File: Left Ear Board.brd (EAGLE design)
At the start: 5 parts

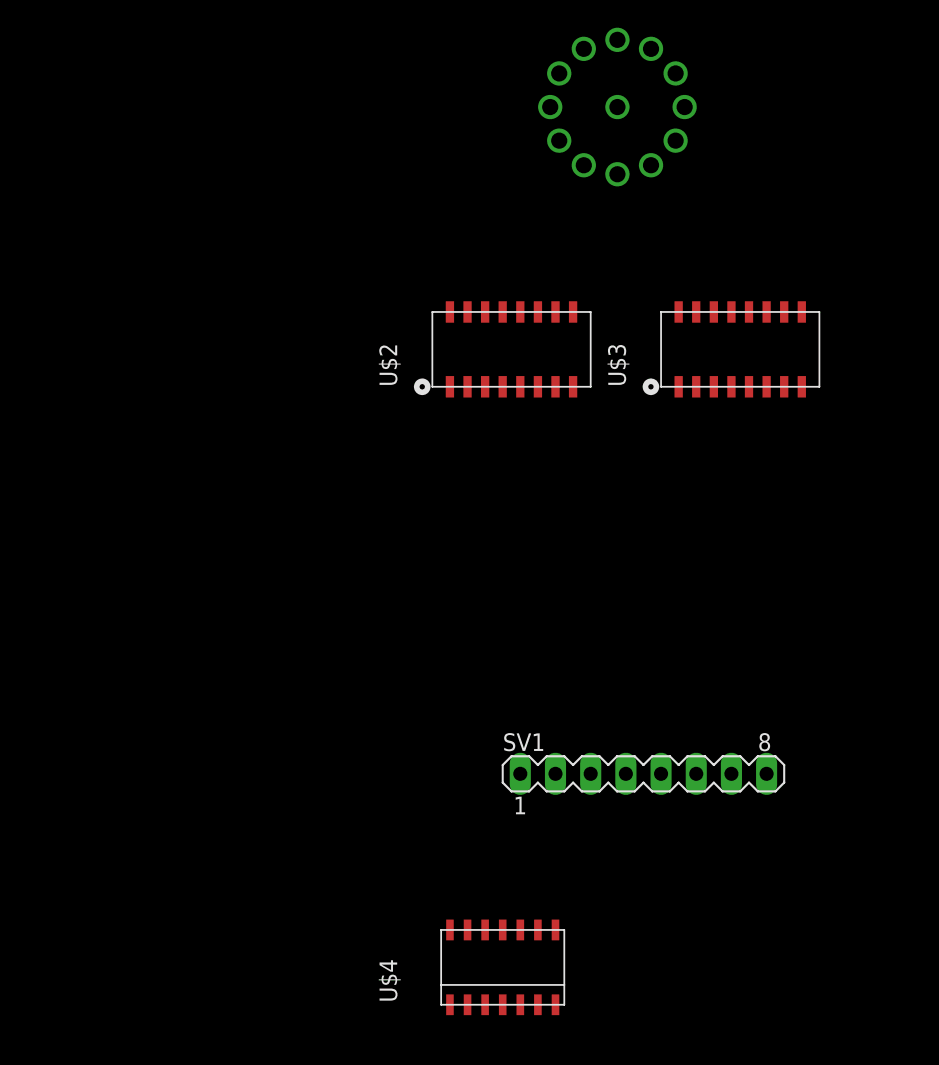
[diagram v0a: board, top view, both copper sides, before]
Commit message: Finished Board Schematic. Routing needs to be done.
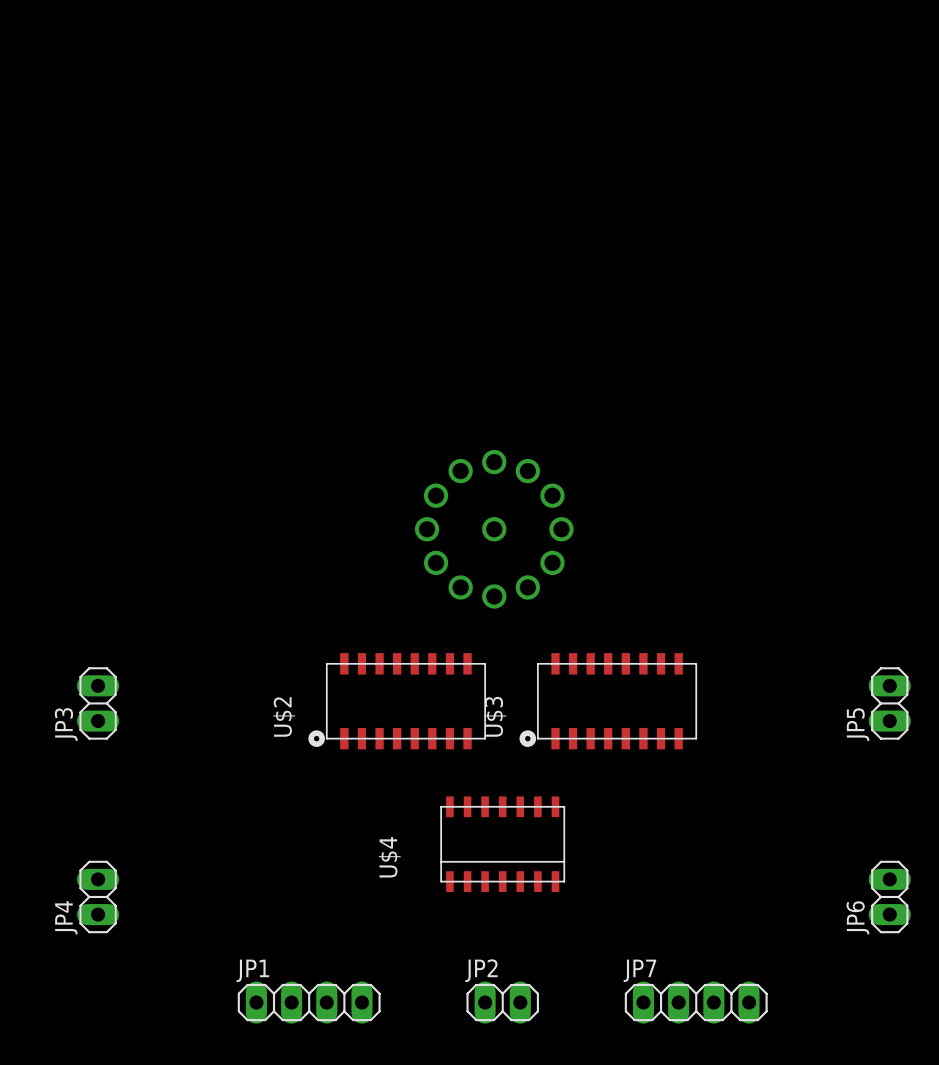
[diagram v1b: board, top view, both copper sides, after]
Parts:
- removed SV1: (no value), con-lstb:MA08-1
- added JP1, JP7: (no value), pinhead:1X04
- added JP2, JP3, JP4, JP5, JP6: (no value), pinhead:1X02
- moved U$1 31.8 mm to (31.8, 34.3)
- moved U$3 26.9 mm to (36.8, 20.3)
- moved U$2 26.5 mm to (21.6, 20.3)
- moved U$4 8.89 mm to (33.0, 12.7)
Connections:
- new net N$22: JP4.1, JP7.2
- new net N$23: JP5.1, JP7.3
- new net N$24: JP6.1, JP7.4
- net 0: now also JP1.1; no longer SV1.7
- net 1: now also JP1.2; no longer SV1.6
- net 2: now also JP1.3; no longer SV1.5
- net 3: now also JP1.4; no longer SV1.4
- net GND: now also JP2.2, JP3.2, JP4.2, JP5.2, JP6.2; no longer SV1.1
- net N$21: now also JP3.1, JP7.1; no longer SV1.3, U$4.3
- net VCC: now also JP2.1; no longer SV1.8

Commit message: Finished board layout
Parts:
- added R1, R10, R11, R12, R2, R3, R4, R5, R6, R7, R8, R9: 10k, rcl:R0603
- moved JP5 34.4 mm to (30.9, 6.05)
- moved JP6 30.3 mm to (30.8, 11.6)
- moved JP7 22.3 mm to (24.7, 2.11)
- moved U$3 19.1 mm to (18.7, 14.5)
- moved U$1 18.5 mm to (15.8, 25.0)
- moved U$2 16.9 mm to (5.77, 14.5)
- moved JP2 16.6 mm to (16.5, 2.11)
- moved U$4 16.6 mm to (17.0, 8.59), turned to 90 degrees
- moved JP3 11.7 mm to (2.21, 11.3)
- moved JP1 10.8 mm to (8.26, 2.06), turned to 180 degrees
- moved JP4 3.52 mm to (2.18, 5.77)
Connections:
- net N$1: now also R1.2
- net N$10: now also R9.1
- net N$11: now also R10.1
- net N$12: now also R11.1
- net N$13: now also R12.1
- net N$14: now also R2.2
- net N$15: now also R3.2
- net N$16: now also R4.2
- net N$17: now also R5.2
- net N$18: now also R6.2
- net N$19: now also R7.2
- net N$20: now also R8.2
- net VCC: now also R1.1, R10.2, R11.2, R12.2, R2.1, R3.1, R4.1, R5.1, R6.1, R7.1, R8.1, R9.2
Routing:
- net VCC: track 0.00 -> 76.2 mm, vias 0 -> 5
- net N$20: track 0.00 -> 49.5 mm, vias 0 -> 4
- net N$19: track 0.00 -> 47.9 mm, vias 0 -> 3
- net N$18: track 0.00 -> 37.7 mm, vias 0 -> 2
- net 3: track 0.00 -> 32.8 mm, vias 0 -> 2
- net N$17: track 0.00 -> 28.3 mm, vias 0 -> 1
- net N$3: track 0.00 -> 26.7 mm, vias 0 -> 2
- net N$21: track 0.00 -> 26.0 mm, vias 0 -> 3
- net N$8: track 0.00 -> 24.9 mm, vias 0 -> 2
- net N$22: track 0.00 -> 22.3 mm, vias 0 -> 2
- net 2: track 0.00 -> 21.5 mm, vias 0 -> 2
- net N$2: track 0.00 -> 20.0 mm, vias 0 -> 2
- net 1: track 0.00 -> 19.1 mm, vias 0 -> 2
- net N$9: track 0.00 -> 16.9 mm
- net N$13: track 0.00 -> 15.8 mm, vias 0 -> 3
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- added copper zone on layer 1, net GND
- added copper zone on layer 16, net GND
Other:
- board outline added: 33 x 32.4 mm
